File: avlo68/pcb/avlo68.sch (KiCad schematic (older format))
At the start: 160 parts, among them P1 OLED, SW1 SW_PUSH, SW10 SW_PUSH, SW11 SW_PUSH, SW12 SW_PUSH, SW13 SW_PUSH, SW14 SW_PUSH, SW15 SW_PUSH, SW16 SW_PUSH, SW17 SW_PUSH, SW18 SW_PUSH, SW19 SW_PUSH, SW2 SW_PUSH, SW20 SW_PUSH, SW21 SW_PUSH, SW22 SW_PUSH, SW23 SW_PUSH, SW24 SW_PUSH, SW25 SW_PUSH, SW26 SW_PUSH, SW27 SW_PUSH, SW28 SW_PUSH, SW29 SW_PUSH, SW3 SW_PUSH, SW30 SW_PUSH, SW31 SW_PUSH, SW32 SW_PUSH, SW33 SW_PUSH, SW34 SW_PUSH, SW35 SW_PUSH, SW36 SW_PUSH, SW37 SW_PUSH, SW38 SW_PUSH, SW39 SW_PUSH, SW4 SW_PUSH, SW40 SW_PUSH, SW41 SW_PUSH, SW42 SW_PUSH, SW43 SW_PUSH, SW44 SW_PUSH, SW45 SW_PUSH, SW46 SW_PUSH, SW47 SW_PUSH, SW48 SW_PUSH, SW49 SW_PUSH, SW5 SW_PUSH, SW50 SW_PUSH, SW51 SW_PUSH, SW52 SW_PUSH, SW53 SW_PUSH, SW54 SW_PUSH, SW55 SW_PUSH, SW56 SW_PUSH, SW57 SW_PUSH, SW58 SW_PUSH, SW59 SW_PUSH, SW6 SW_PUSH, SW60 SW_PUSH, SW61 SW_PUSH, SW62 SW_PUSH, SW63 SW_PUSH, SW64 SW_PUSH, SW65 SW_PUSH, SW66 SW_PUSH, SW67 SW_PUSH, SW68 SW_PUSH, SW7 SW_PUSH, SW8 SW_PUSH, SW9 SW_PUSH, U1 ProMicro

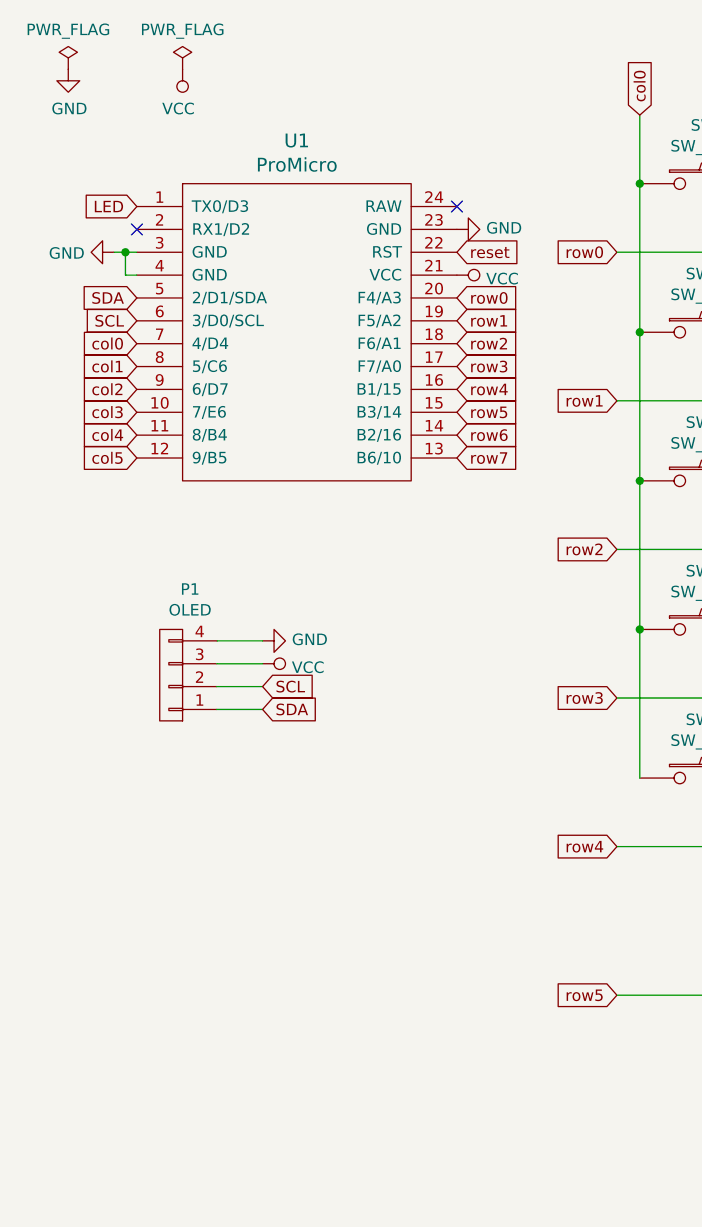
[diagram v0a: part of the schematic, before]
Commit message: Add Black Pill footprint and schematic. Drop Black Pill onto avlo68 schematic.
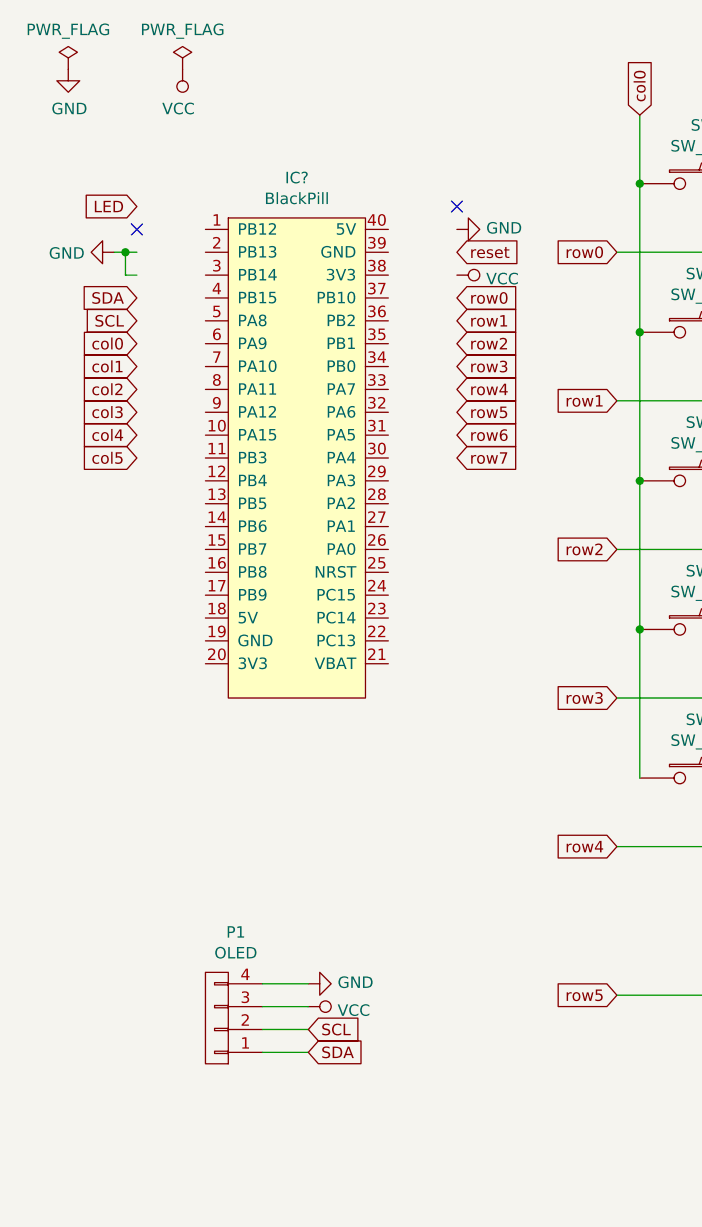
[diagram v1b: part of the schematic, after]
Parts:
- removed U1: ProMicro, avlo-parts:ArduinoProMicro, symbol avlo68-rescue:ProMicro-_reviung-kbd
- added IC?: BlackPill, symbol blackpill:BlackPill
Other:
- moved on the sheet: P1
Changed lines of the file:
@@
-$EndComp
-$Comp
-L avlo68-rescue:ProMicro-_reviung-kbd U1
-U 1 1 5DCBB133
-P 1800 2200
-F 0 "U1" H 1800 3237 60  0000 C CNN
-F 1 "ProMicro" H 1800 3131 60  0000 C CNN
-F 2 "avlo-parts:ArduinoProMicro" H 1900 1150 60  0001 C CNN
-F 3 "" H 1900 1150 60  0000 C CNN
-	1    1800 2200
-	1    0    0    -1
 $EndComp
 $Comp
@@
 L avlo68-rescue:CONN_01X04-Lily58-cache-Lily58-rescue P1
 U 1 1 60A17BDA
-P 1250 3500
-F 0 "P1" H 1167 3125 50  0000 C CNN
-F 1 "OLED" H 1167 3216 50  0000 C CNN
-F 2 "avlo-parts:OLED_4Pin" H 1250 3500 50  0001 C CNN
-F 3 "" H 1250 3500 50  0000 C CNN
-	1    1250 3500
+P 1450 5000
+F 0 "P1" H 1367 4625 50  0000 C CNN
+F 1 "OLED" H 1367 4716 50  0000 C CNN
+F 2 "avlo-parts:OLED_4Pin" H 1450 5000 50  0001 C CNN
+F 3 "" H 1450 5000 50  0000 C CNN
+	1    1450 5000
 	-1   0    0    1
 $EndComp
@@
 L power:VCC #PWR0102
 U 1 1 60A22C43
-P 1650 3450
-F 0 "#PWR0102" H 1650 3300 50  0001 C CNN
-F 1 "VCC" V 1667 3578 50  0000 L CNN
-F 2 "" H 1650 3450 50  0001 C CNN
-F 3 "" H 1650 3450 50  0001 C CNN
-	1    1650 3450
+P 1850 4950
+F 0 "#PWR0102" H 1850 4800 50  0001 C CNN
+F 1 "VCC" V 1867 5078 50  0000 L CNN
+F 2 "" H 1850 4950 50  0001 C CNN
+F 3 "" H 1850 4950 50  0001 C CNN
+	1    1850 4950
 	0    1    1    0
 $EndComp
 Wire Wire Line
-	1450 3450 1650 3450
-Wire Wire Line
-	1450 3550 1650 3550
-Wire Wire Line
-	1450 3650 1650 3650
-Text GLabel 1650 3550 2    50   Input ~ 0
+	1650 4950 1850 4950
+Wire Wire Line
+	1650 5050 1850 5050
+Wire Wire Line
+	1650 5150 1850 5150
+Text GLabel 1850 5050 2    50   Input ~ 0
 SCL
-Text GLabel 1650 3650 2    50   Input ~ 0
+Text GLabel 1850 5150 2    50   Input ~ 0
 SDA
 Text GLabel 1100 1950 0    50   Input ~ 0
@@
 $EndComp
 Wire Wire Line
-	1450 3350 1650 3350
+	1650 4850 1850 4850
 $Comp
 L power:GND #PWR?
 U 1 1 60B41A07
-P 1650 3350
-F 0 "#PWR?" H 1650 3100 50  0001 C CNN
-F 1 "GND" V 1655 3222 50  0000 R CNN
-F 2 "" H 1650 3350 50  0001 C CNN
-F 3 "" H 1650 3350 50  0001 C CNN
-	1    1650 3350
+P 1850 4850
+F 0 "#PWR?" H 1850 4600 50  0001 C CNN
+F 1 "GND" V 1855 4722 50  0000 R CNN
+F 2 "" H 1850 4850 50  0001 C CNN
+F 3 "" H 1850 4850 50  0001 C CNN
+	1    1850 4850
 	0    -1   -1   0
 $EndComp
@@
 Wire Wire Line
 	3200 4900 5900 4900
+$Comp
+L blackpill:BlackPill IC?
+U 1 1 629D46E4
+P 1800 2550
+F 0 "IC?" H 1800 3775 50  0000 C CNN
+F 1 "BlackPill" H 1800 3684 50  0000 C CNN
+F 2 "" H 1500 1350 50  0001 L CNN
+F 3 "" H 1500 1250 50  0001 L CNN
+	1    1800 2550
+	1    0    0    -1
+$EndComp
 $EndSCHEMATC

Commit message: Add rotary encoders and OLED to schematic
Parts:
- removed P1: OLED, avlo-parts:OLED_4Pin, symbol avlo68-rescue:CONN_01X04-Lily58-cache-Lily58-rescue
- added Brd1: SSD1306, symbol ssd1306:SSD1306
- added D61, D?: 1N4148W, avlo-parts:Diode-dual, symbol Diode:1N4148W
- added SW61, SW70: Rotary_Encoder_Switch, symbol Device:Rotary_Encoder_Switch
- gave numbers to parts that had none: 1
- renumbered D61 to D62, D62 to D63, D63 to D64, D64 to D65, D65 to D66, D66 to D67, D67 to D68, D68 to D69, SW61 to SW62, SW62 to SW63, SW63 to SW64, SW64 to SW65, SW65 to SW66, SW66 to SW67, SW67 to SW68, SW68 to SW69
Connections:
- net col1 is gone; now on net SW61A: SW14.1, SW2.1, SW26.1, SW38.1, SW50.1
- net col10 is gone; now on net SW70A: SW11.1, SW23.1, SW35.1, SW47.1, SW59.1
- net GND: now also IC0.19 (GND), IC0.39 (GND), Brd1.1 (GND), SW61.C, SW70.C
- net SCL: now also IC0.29 (PA3), Brd1.3 (SCL)
- net SDA: now also IC0.28 (PA2), Brd1.4 (SDA)
- net VCC: now also IC0.18 (5V), IC0.40 (5V), Brd1.2 (VCC)
- net col0: now also IC0.7 (PA10)
- net col11: now also IC0.32 (PA6)
- net col2: now also IC0.9 (PA12)
- net col3: now also IC0.10 (PA15)
- net col4: now also IC0.11 (PB3)
- net col5: now also IC0.12 (PB4)
- net col6: now also IC0.37 (PB10)
- net col7: now also IC0.36 (PB2)
- net col8: now also IC0.35 (PB1)
- net col9: now also IC0.34 (PB0)
- net reset: now also IC0.25 (NRST)
- net row0: now also IC0.1 (PB12)
- net row1: now also IC0.2 (PB13)
- net row2: now also IC0.3 (PB14)
- net row3: now also IC0.4 (PB15)
- net row4: now also IC0.5 (PA8)
- net row5: now also IC0.6 (PA9), D61.1 (K), D?.1 (K)
- net ENC61A: now reaches IC0.13 (PB5)
- net ENC61A: now also SW61.A
- net ENC61B: now reaches IC0.14 (PB6)
- net ENC61B: now also SW61.B
- net ENC70B: now reaches IC0.30 (PA4)
- net ENC70B: now also SW70.B
- net ENC70A: now reaches IC0.31 (PA5)
- net ENC70A: now also SW70.A
- net SW70A: now reaches IC0.33 (PA7)
- net SW70A: now also SW70.S1
- net SW61A: now reaches IC0.8 (PA11)
- net SW61A: now also SW61.S1
- new net SW61B: D61.2 (A), SW61.S2
- new net SW70B: D?.2 (A), SW70.S2
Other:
- moved on the sheet: RESET1
